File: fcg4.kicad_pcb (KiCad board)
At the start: 4 copper layers, 34 x 33.5 mm, 99 parts, among them IC1 MP9943AGQ-Z, IC2 MP9943AGQ-Z, J1 USB4105-GF-A-120, J2 SM08B-SRSS-TB, U1 STM32G473CEUx, U10 MAX40200ANS_T, U11 MAX40200ANS_T, U2 ICM-42688-P, U4 AP2112K-3.3TRG1, U5 AP2112K-1.8TRG1, Y1 ECS-240-6-37B-7KM-TR

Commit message: routing...
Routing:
- net /Power/VOUT: track 0.00 -> 1.73 mm

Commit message: routing
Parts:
- added TP1: TestPoint, TestPoint:TestPoint_Pad_D1.0mm, F.Cu at (24.2, 21.7)
- added TP2: TestPoint, TestPoint:TestPoint_Pad_D1.0mm, F.Cu at (24.3, 24.0)
- added TP3: TestPoint, TestPoint:TestPoint_Pad_D1.0mm, F.Cu at (24.8, 31.1)
- added TP4: TestPoint, TestPoint:TestPoint_Pad_D1.0mm, F.Cu at (8.20, 3.70)
- added TP5: TestPoint, TestPoint:TestPoint_Pad_D1.0mm, F.Cu at (7.80, 5.80)
- added TP6: TestPoint, TestPoint:TestPoint_Pad_D1.0mm, F.Cu at (10.9, 4.70)
- added TP7: TestPoint, TestPoint:TestPoint_Pad_D1.0mm, F.Cu at (9.80, 6.50)
- added TP8: TestPoint, TestPoint:TestPoint_Pad_D1.0mm, F.Cu at (9.30, 14.5)
- moved C9 1.22 mm to (15.4, 14.1), turned to 180 degrees
- moved C8 0.82 mm to (15.4, 15.1), turned to 180 degrees
- moved R18 0.51 mm to (18.5, 13.7)
- moved C31 0.50 mm to (21.0, 14.2)
- moved R16 0.50 mm to (20.0, 14.2)
- moved R17 0.50 mm to (22.0, 14.2)
- moved C23 0.49 mm to (18.5, 14.7)
- moved C26 0.45 mm to (9.48, 24.2)
- moved C28 0.45 mm to (9.50, 23.2)
- moved C24 0.26 mm to (19.9, 27.1)
- moved C25 0.24 mm to (20.9, 27.1)
- moved FL1 0.20 mm to (20.5, 25.3)
- moved C20 0.10 mm to (7.60, 19.9)
- turned H1 to 90 degrees
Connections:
- net BEEPER renamed BZ
- C21 pad 1: /Power/VOUT -> VCC_ICM
- U1 pad 36: PINIO1 -> SWDIO-JTMS
- U1 pad 37: unconnected-(U1-PA14-Pad37) -> SWCLK-JTCK
- U5 pad 5: /Power/VOUT -> VCC_ICM
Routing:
- net /Connectors/MOTOR_2: track 2.10 -> 24.8 mm, vias 0 -> 2
- net /Connectors/MOTOR_1: track 2.17 -> 24.1 mm, vias 0 -> 2
- net /Connectors/MOTOR_4: track 1.82 -> 21.5 mm, vias 0 -> 2
- net /Connectors/MOTOR_3: track 1.90 -> 20.0 mm, vias 0 -> 2
- net SWCLK-JTCK: track 0.00 -> 10.8 mm, vias 0 -> 2
- net SWDIO-JTMS: track 0.00 -> 9.74 mm, vias 0 -> 2
- net GND: track 70.3 -> 73.3 mm, vias 28 -> 46
- net 5V5_BEC: track 8.00 -> 10.6 mm
- net /Power/BIAS_SUPPLY_5V5: track 3.83 -> 1.83 mm
- net I2C1_SCL: track 43.5 -> 45.2 mm
- net /Power/VOUT: track 1.73 -> 0.00 mm
- net I2C1_SDA: track 26.0 -> 27.5 mm
- net /Power/RC_BST_5V5: track 0.96 -> 0.00 mm
- net TX4: track 23.1 -> 22.6 mm
- net TX3: track 30.1 -> 29.6 mm
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
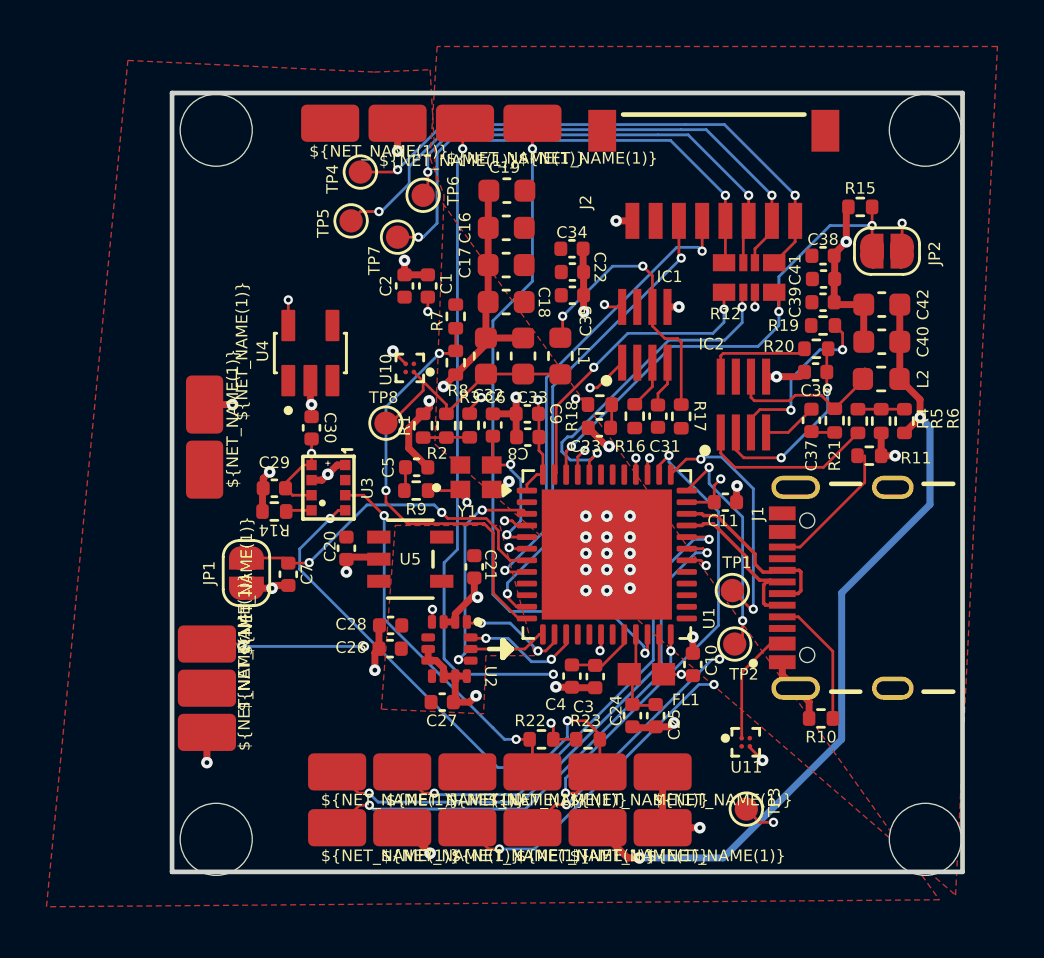
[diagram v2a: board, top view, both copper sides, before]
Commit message: Update board settings and design rules in KiCad project files
- Changed active layer from 0 to 2 and disabled auto track width in fcg4.kicad_prl.
- Adjusted column widths for better layout in fcg4.kicad_prl.
- Increased silk text size and thickness for improved visibility in fcg4.kicad_pro.
- Changed track and via dangling rules from warning to error for stricter design checks in fcg4.kicad_pro.
- Updated minimum hole-to-hole clearance and via annular width for enhanced manufacturability in fcg4.kicad_pro.
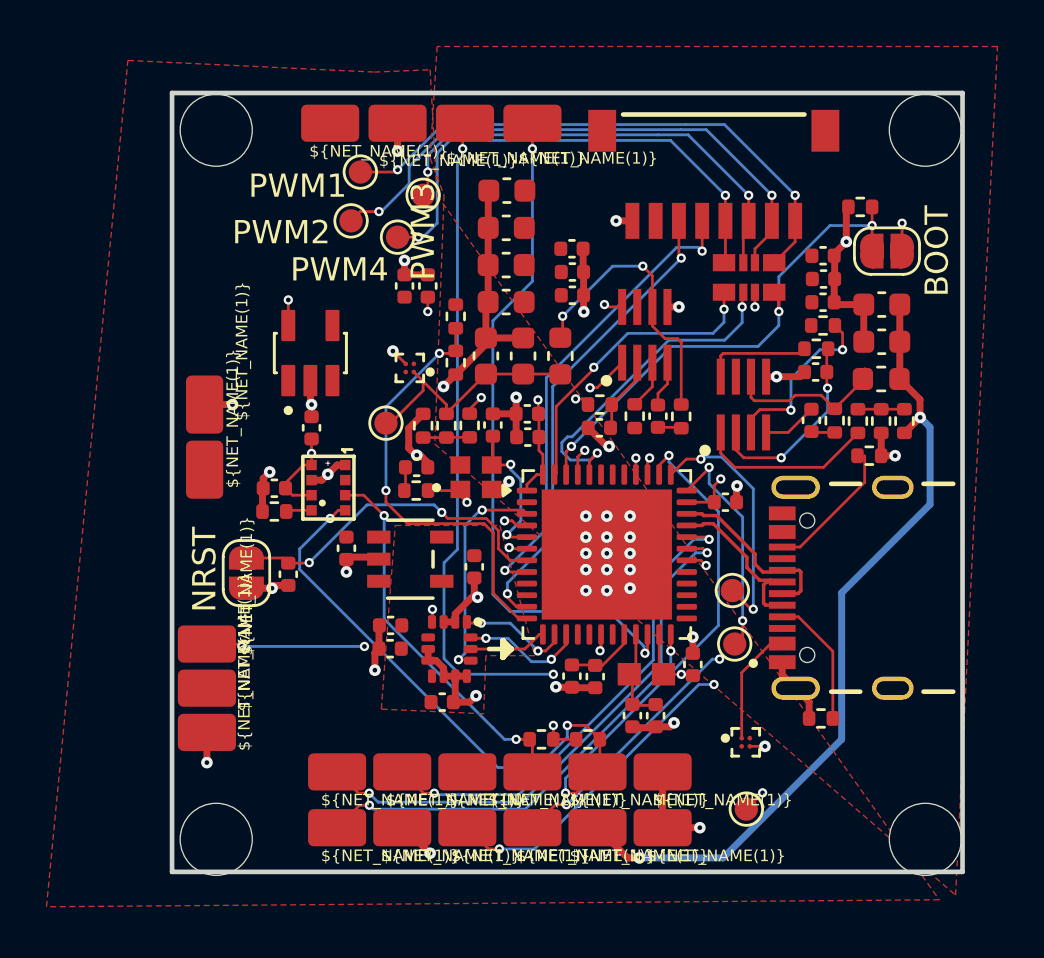
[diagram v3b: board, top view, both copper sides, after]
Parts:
- JP1: value SolderJumper_2_Open -> NRST
- JP2: value SolderJumper_2_Open -> BOOT
- TP4: value TestPoint -> PWM1
- TP5: value TestPoint -> PWM2
- TP6: value TestPoint -> PWM3
- TP7: value TestPoint -> PWM4
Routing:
- net /Power/BIAS_SUPPLY_5V5: track 1.83 -> 4.09 mm
- net /Power/RC_BST_5V5: track 0.00 -> 1.02 mm
- net GND: track 73.3 -> 72.6 mm
- net VDD_MCU: track 20.4 -> 19.8 mm

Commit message: Update footprint references and component values in schematic files
- Changed footprint property for a component in mcu.kicad_sch from "Package_DFN_QFN:QFN-48-1EP_7x7mm_P0.5mm_EP5.6x5.6mm" to "fcg4_fp:QFN-48-1EP_7x7mm_P0.5mm_EP5.6x5.6mm".
- Updated value property for a component in mcu.kicad_sch from "SolderJumper_2_Open" to "BOOT".
- Changed value property for another component in mcu.kicad_sch from "SolderJumper_2_Open" to "RESET".
- Modified footprint property for a component in sensor.kicad_sch from "ProLib_pcs_2026-02-12:SENSOR-SMD_SPL06-001" to "fcg4_fp:SENSOR-SMD_SPL06-001".
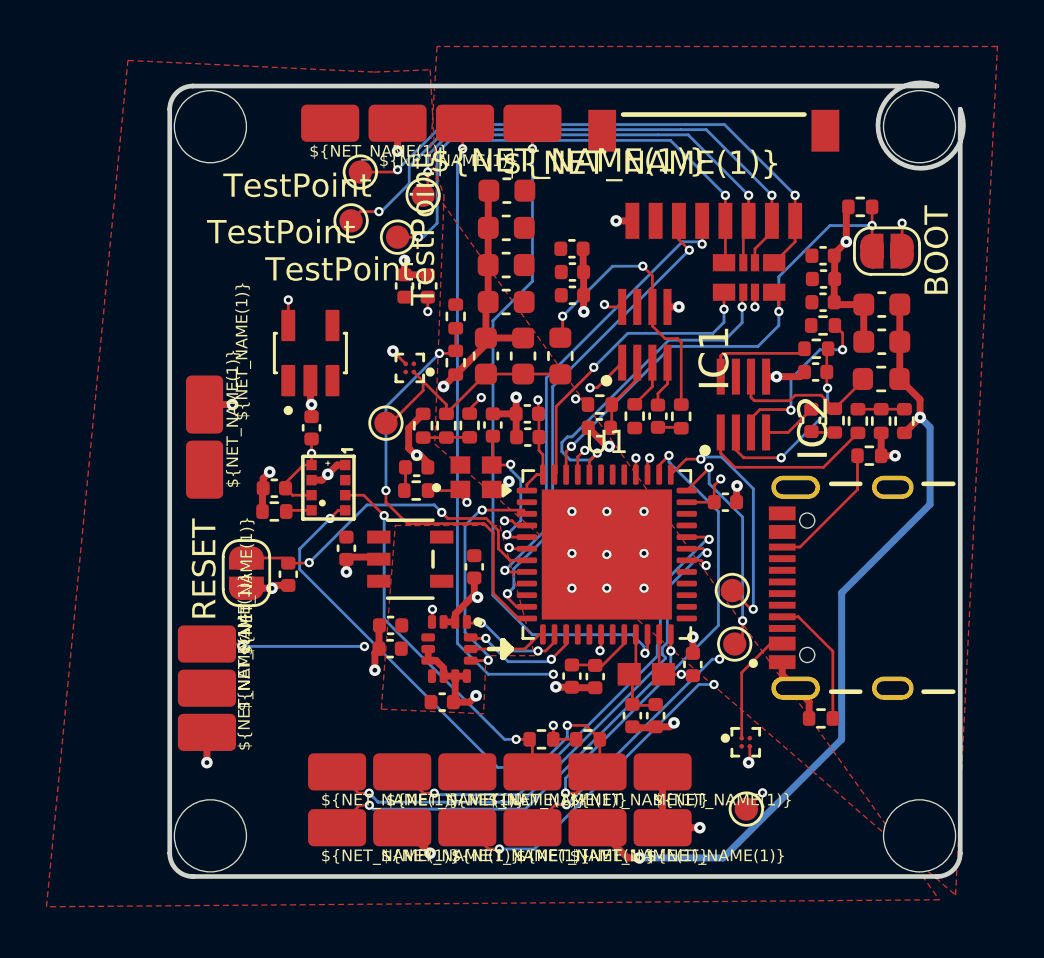
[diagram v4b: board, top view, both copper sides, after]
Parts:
- JP1: value NRST -> RESET
- TP4: value PWM1 -> TestPoint
- TP5: value PWM2 -> TestPoint
- TP6: value PWM3 -> TestPoint
- TP7: value PWM4 -> TestPoint
- U1: footprint Package_DFN_QFN:QFN-48-1EP_7x7mm_P0.5mm_EP5.6x5.6mm -> fcg4_fp:QFN-48-1EP_7x7mm_P0.5mm_EP5.6x5.6mm
- moved H1 0.29 mm to (17.0, 17.0)
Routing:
- net /MCU/USB_DIFF+: track 7.92 -> 0.00 mm
- net /MCU/USB_DIFF-: track 7.91 -> 0.00 mm
- net RX3: track 53.0 -> 51.8 mm
- net GYRO_1_CS: track 9.43 -> 9.98 mm
- net GND: track 72.6 -> 72.7 mm, vias 46 -> 40
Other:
- board size 34 x 33.5 mm -> 34.1 x 34.1 mm

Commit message: update routing and pcb cuts edge
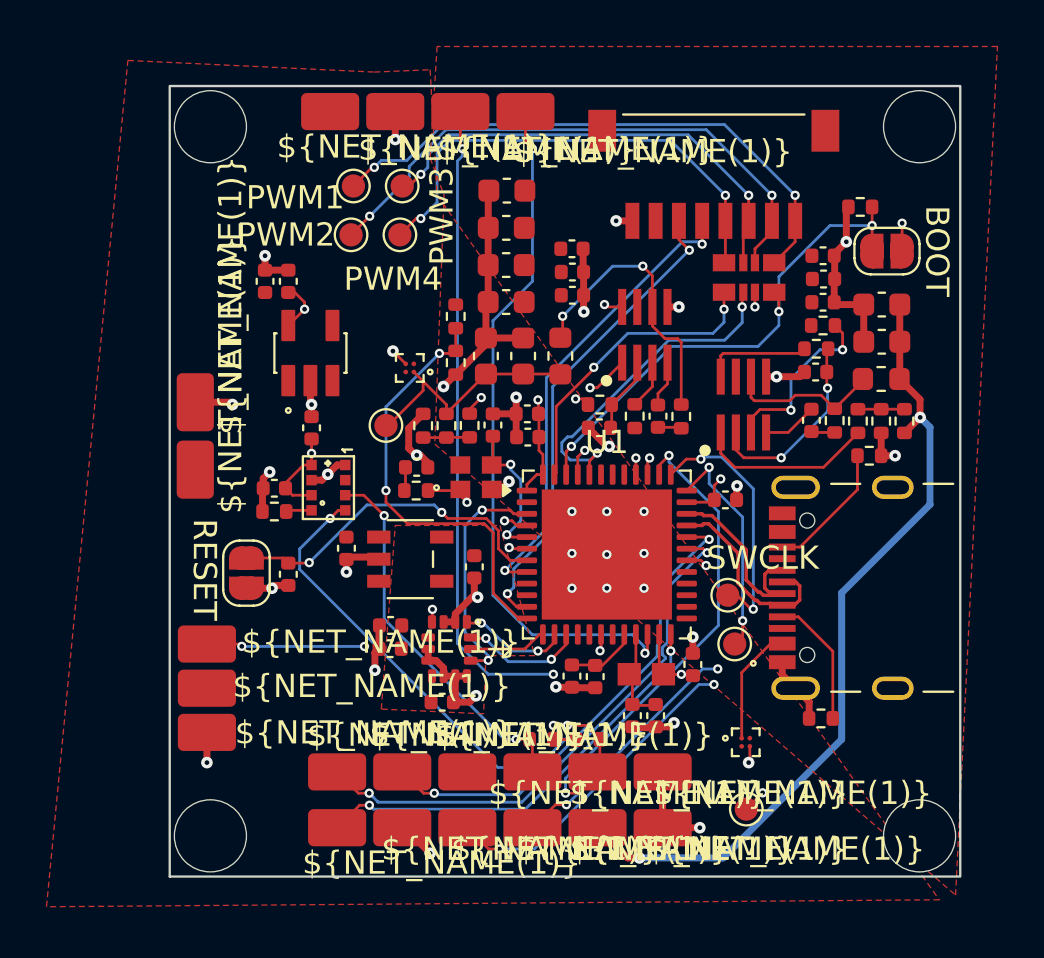
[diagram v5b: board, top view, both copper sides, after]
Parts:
- TP1: value TestPoint -> SWCLK
- TP2: value TestPoint -> SWDIO
- TP3: value TestPoint -> VDD_MCU
- TP4: value TestPoint -> PWM1
- TP5: value TestPoint -> PWM2
- TP6: value TestPoint -> PWM3
- TP7: value TestPoint -> PWM4
- TP8: value TestPoint -> 5V_BEC
- moved C1 6.00 mm to (5.10, 8.40)
- moved C2 6.00 mm to (4.10, 8.40)
- moved TP6 0.98 mm to (10.0, 4.30)
- moved TP4 0.67 mm to (7.90, 4.30)
- moved TP5 0.60 mm to (7.80, 6.40)
- moved U14 0.58 mm to (15.3, 1.10)
- moved U15 0.54 mm to (12.5, 1.10)
- moved U17 0.51 mm to (9.70, 1.10)
- moved U16 0.50 mm to (6.90, 1.10)
- moved U19 0.41 mm to (1.10, 13.6)
- moved U18 0.40 mm to (1.10, 16.5)
- moved TP1 0.28 mm to (24.0, 21.9)
- moved TP7 0.14 mm to (9.90, 6.40)
- moved TP8 0.10 mm to (9.30, 14.6)
- moved C11 0.10 mm to (23.9, 17.8)
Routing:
- net /MCU/USB_DIFF-: track 0.00 -> 8.62 mm
- net /MCU/USB_DIFF+: track 0.00 -> 8.61 mm
- net /Connectors/MOTOR_4: track 21.5 -> 20.8 mm
- net TX3: track 29.6 -> 30.2 mm
- net /Connectors/MOTOR_1: track 24.1 -> 24.6 mm
- net RX3: track 51.8 -> 52.3 mm
- net VDD_MCU: track 19.8 -> 20.2 mm, vias 9 -> 8
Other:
- board size 34.1 x 34.1 mm -> 34 x 34 mm

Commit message: Add new Gerber job file for fcg4 project with complete specifications and material stackup
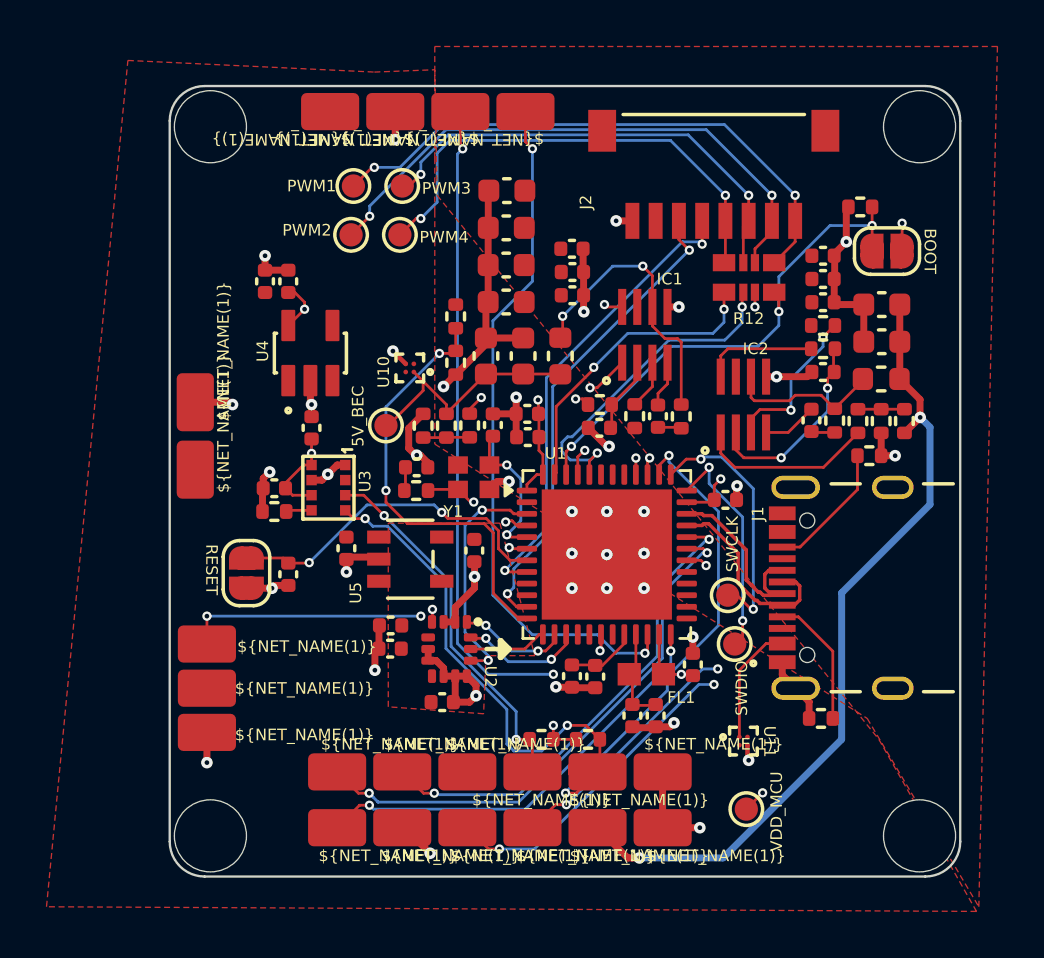
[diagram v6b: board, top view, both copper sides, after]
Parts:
- moved C21 0.70 mm to (13.1, 20.0)
- moved C36 0.32 mm to (28.1, 12.3)
- moved R20 0.29 mm to (28.1, 11.3)
- moved U11 0.11 mm to (24.7, 28.2)
- moved Y1 0.10 mm to (13.1, 16.8)
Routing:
- net I2C1_SCL: track 44.8 -> 42.0 mm
- net GND: track 73.0 -> 74.8 mm
- net /Power/EN/SYNC_9V: track 7.76 -> 6.92 mm
- net BZ: track 24.0 -> 24.7 mm
- net /Power/PG_9V: track 4.62 -> 5.19 mm
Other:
- outline, holes or cut-outs redrawn
- board text added: "FCG4 V1.0 by Max Dev"

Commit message: Update KiCad project files and component specifications
- Modified visible layers in fcg4.kicad_prl to adjust layer visibility settings.
- Increased via diameter and drill size in fcg4.kicad_pro for improved connectivity.
- Adjusted soldering pad dimensions in soldering_pad.kicad_mod for better fit.
- Updated fp-info-cache with new identifier for BatteryClip_Keystone_54_D16-19mm.
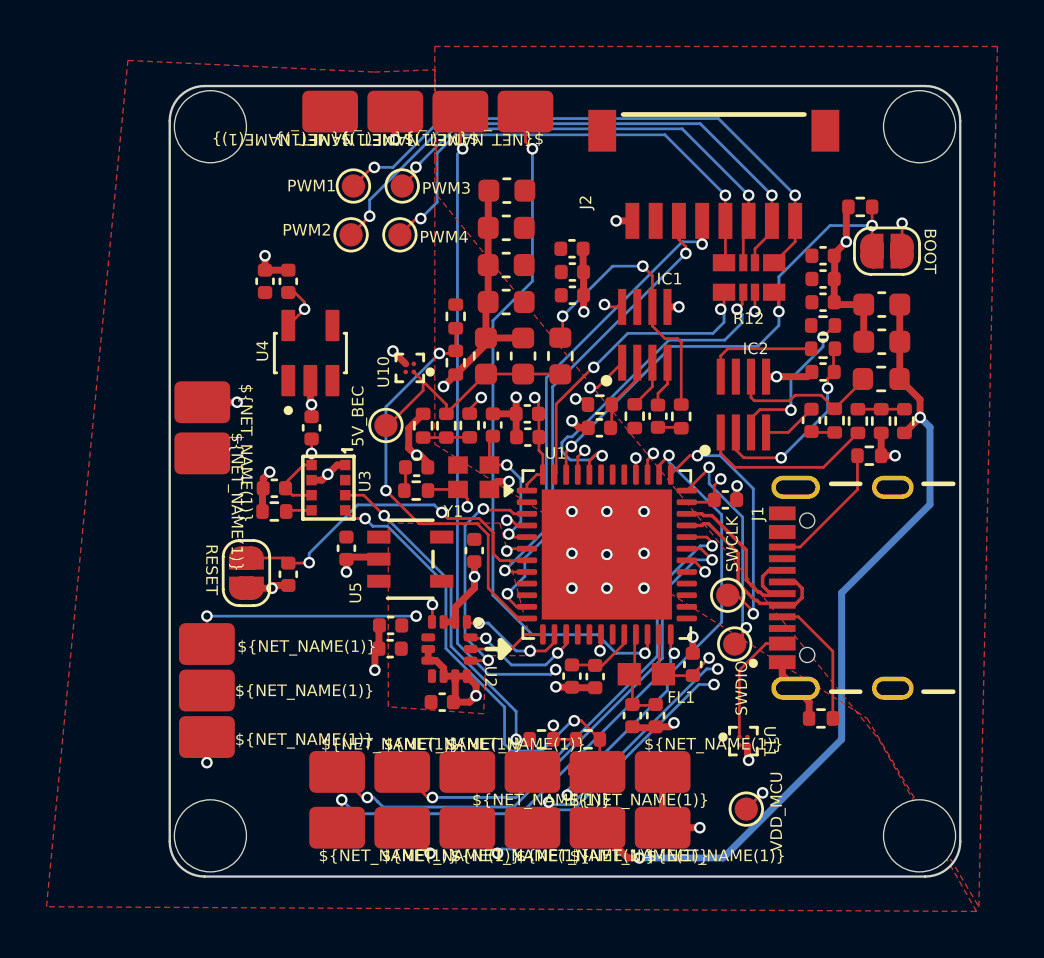
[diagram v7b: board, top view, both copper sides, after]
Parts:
- moved U18 0.76 mm to (1.40, 15.8), turned to 180 degrees
- moved U19 0.30 mm to (1.40, 13.6), turned to 180 degrees
- moved U25 0.20 mm to (1.60, 28.0)
- moved U24 0.10 mm to (1.60, 26.0)
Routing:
- net RX3: track 52.3 -> 53.5 mm
- net VDD_MCU: track 20.2 -> 21.2 mm
- net TX4: track 22.8 -> 23.5 mm
- net /MCU/OSC_OUT: track 7.46 -> 8.16 mm
- net TX1: track 23.5 -> 24.1 mm
- net MOTOR3: track 14.5 -> 15.1 mm
- net GND: track 74.8 -> 74.3 mm
